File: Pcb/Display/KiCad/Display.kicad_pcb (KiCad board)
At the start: 2 copper layers, 63.5 x 76.4 mm, 31 parts, among them J2 47219-2001, Q1 310mA/60V/1.6Ω

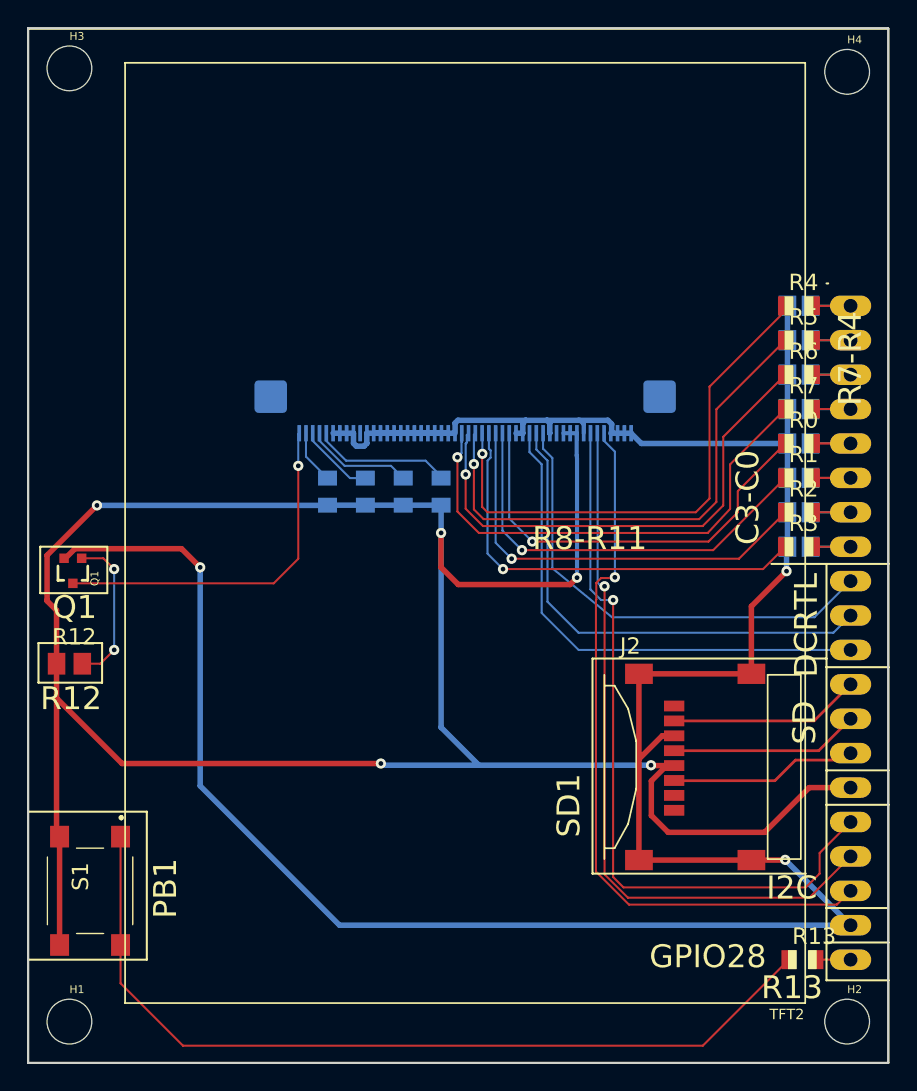
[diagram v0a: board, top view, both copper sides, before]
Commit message: Updated PCB files and ported some of the graphics functions. The graphics changes are not tested yet.
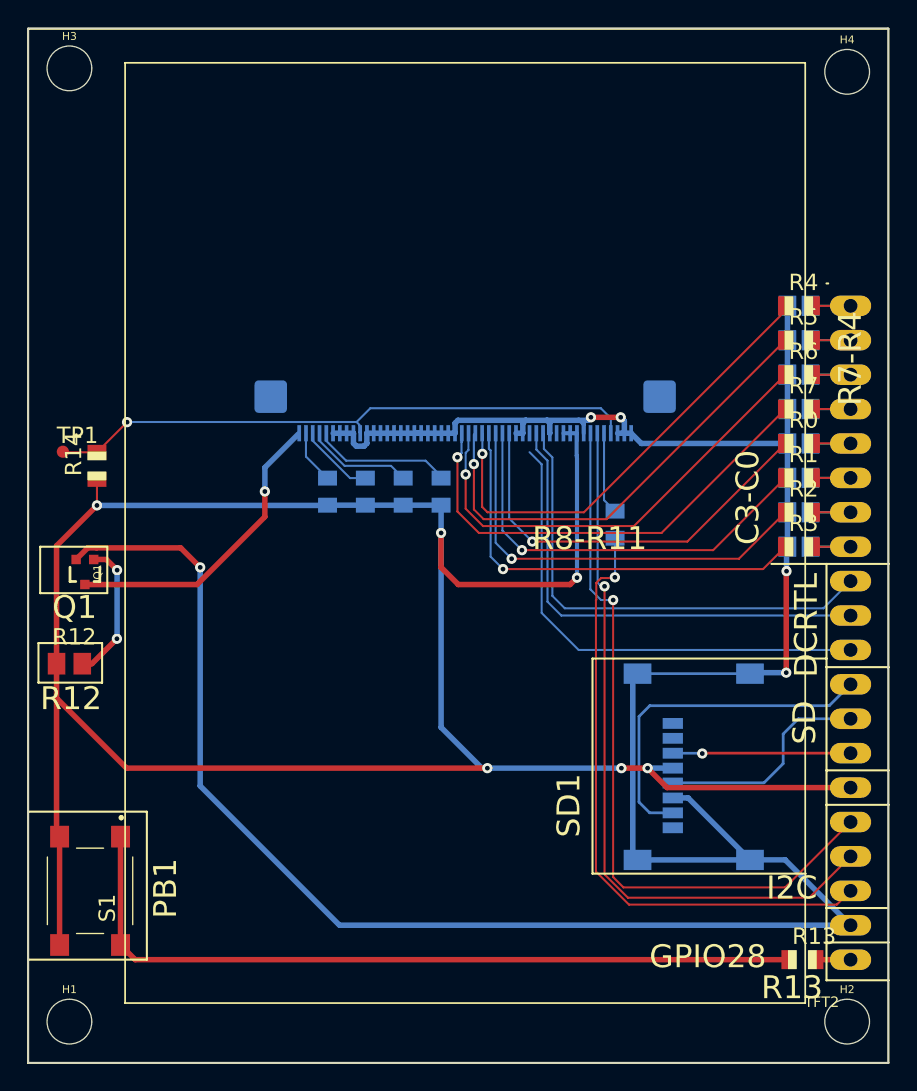
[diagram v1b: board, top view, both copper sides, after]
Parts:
- added R14: 10, Display:R0805, F.Cu at (121.8, 99.1)
- added R15: 1k, Display:R0805, B.Cu at (160.1, 103.5)
- added TP1: TPTP09R, Display:TP09R, F.Cu at (119.3, 98.1)
- J2: moved to B.Cu
- moved Q1 0.89 mm to (121.0, 107.0)
- moved J2 0.10 mm to (166.4, 121.3), turned to 90 degrees
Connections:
- JP4 pad 10: /WRX -> Net-(JP4-Pad10)
- JP4 pad 11: /RDX -> Net-(JP4-Pad11)
- TFT2 pad 10: Net-(TFT2-Pad10) -> /RST
- TFT2 pad 35: /WRX -> Net-(JP4-Pad11)
- TFT2 pad 36: /RDX -> Net-(JP4-Pad10)
- TFT2 pad 46: /I2C_INT -> Net-(R15-Pad2)
- TFT2 pad 47: GND -> /RST
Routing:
- net GND: track 257.9 -> 198.2 mm, vias 3 -> 5
- net /RST: track 0.00 -> 44.2 mm, vias 0 -> 1
- net /WRX: track 37.6 -> 0.00 mm
- net /RDX: track 36.6 -> 0.00 mm
- net Net-(JP4-Pad10): track 0.00 -> 36.2 mm
- net Net-(JP4-Pad11): track 0.00 -> 35.6 mm
- net /SD_DAT0: track 14.1 -> 25.7 mm
- net /I2C_INT: track 54.0 -> 46.0 mm
- net /R13: track 64.7 -> 57.8 mm
- net Net-(R15-Pad2): track 0.00 -> 6.09 mm
- net Net-(R4-Pad1): track 39.4 -> 34.5 mm
- net VCC: track 183.8 -> 179.0 mm, vias 5 -> 6
- net /R12: track 26.7 -> 22.6 mm
- net Net-(R5-Pad1): track 38.4 -> 34.4 mm
- net Net-(R6-Pad1): track 37.4 -> 34.4 mm
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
